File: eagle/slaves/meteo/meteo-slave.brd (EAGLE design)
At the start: 49.5 x 49.5 mm, 38 parts, among them CON1 SPI, IC1 MCP1703CB, J2 RJ12RIGHTANGLE-I2C, J3 RJ12RIGHTANGLE-I2C, U1 ATMEGA328P_TQFP, X1 8MHz, X2 1503_09, X3 1503_09

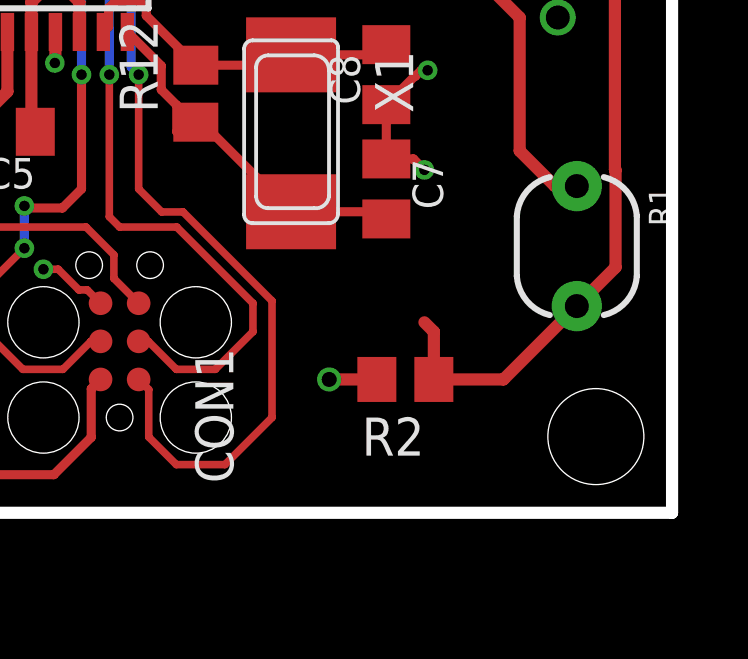
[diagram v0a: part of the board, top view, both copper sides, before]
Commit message: meteo-slave: change light control to use internal pullup
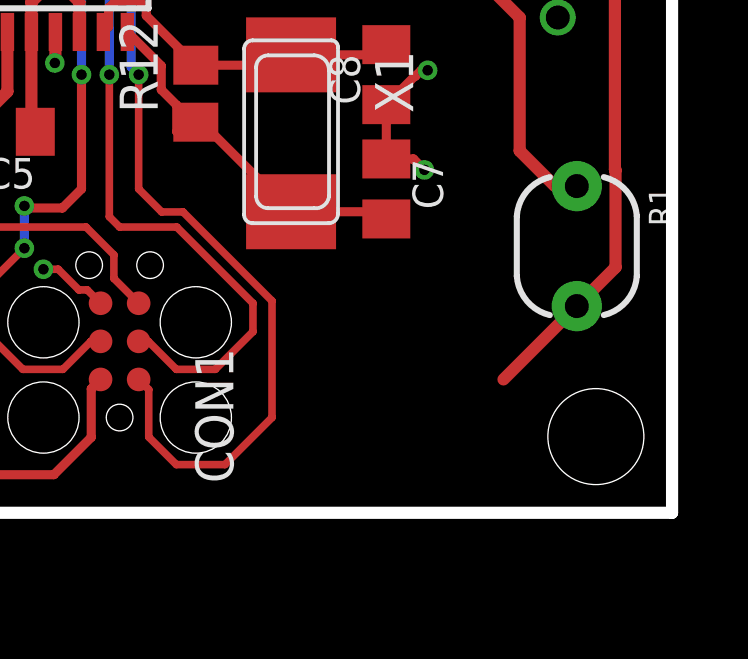
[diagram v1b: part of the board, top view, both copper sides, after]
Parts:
- removed R2: 10k, resistor:R0805
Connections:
- net A0: no longer R2.1
- net D5: no longer R1.1
- net GND: now also R1.1; no longer R2.2
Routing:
- net A0: track 54.2 -> 49.8 mm
- net GND: track 32.5 -> 30.9 mm, vias 12 -> 11
- net D5: track 18.8 -> 18.1 mm
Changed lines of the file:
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@@
 </element>
 <element name="R1" library="SparkFun" package="PHOTOCELL" value="PHOTOCELLPTH" x="46.355" y="8.89" rot="R270"/>
-<element name="R2" library="resistor" library_urn="urn:adsk.eagle:library:348" package="R0805" value="10k" x="40.64" y="4.445" rot="R180"/>
 <element name="U$1" library="Ava" package="DS1820" value="DS1820TO92" x="46.99" y="40.64" rot="R270"/>
 <element name="R4" library="resistor" library_urn="urn:adsk.eagle:library:348" package="R0805" value="4.7k" x="45.72" y="33.02" smashed="yes">
@@
 <contactref element="U$1" pad="GND"/>
 <contactref element="U2" pad="GND"/>
-<contactref element="R2" pad="2"/>
 <contactref element="U$19" pad="GND"/>
 <contactref element="X2" pad="3"/>
@@
 <wire x1="42.529" y1="20.336" x2="42.545" y2="20.32" width="0.4064" layer="1"/>
 <via x="42.545" y="20.32" extent="1-16" drill="0.5"/>
-<wire x1="39.69" y1="4.445" x2="38.1" y2="4.445" width="0.4064" layer="1"/>
-<via x="38.1" y="4.445" extent="1-16" drill="0.5"/>
 <wire x1="7.874" y1="39.37" x2="7.874" y2="37.719" width="0.4064" layer="1"/>
 <wire x1="7.874" y1="37.719" x2="7.62" y2="37.465" width="0.4064" layer="1"/>
@@
 <contactref element="R19" pad="1"/>
 <contactref element="C11" pad="1"/>
+<contactref element="R1" pad="1"/>
 <wire x1="41.245" y1="38.36" x2="45.72" y2="40.005" width="0" layer="19" extent="1-1"/>
 <wire x1="29.21" y1="31.877" x2="41.245" y2="38.36" width="0" layer="19" extent="16-16"/>
@@
 <wire x1="24.13" y1="4.445" x2="28.575" y2="8.1188" width="0" layer="19" extent="1-1"/>
 <wire x1="21.59" y1="4.445" x2="24.13" y2="4.445" width="0" layer="19" extent="1-1"/>
-<wire x1="38.1" y1="4.445" x2="30.48" y2="6.985" width="0" layer="19" extent="1-1"/>
-<wire x1="41.275" y1="11.43" x2="39.69" y2="4.445" width="0" layer="19" extent="1-1"/>
+<wire x1="6.745" y1="16.51" x2="16.51" y2="19.685" width="0" layer="19" extent="1-1"/>
+<wire x1="6.745" y1="14.47" x2="6.745" y2="16.51" width="0" layer="19" extent="1-1"/>
+<wire x1="40.005" y1="11.795" x2="30.48" y2="6.985" width="0" layer="19" extent="1-1"/>
 <wire x1="45.72" y1="16.51" x2="41.3824" y2="14.7506" width="0" layer="19" extent="1-1"/>
 <wire x1="42.545" y1="20.32" x2="45.72" y2="16.51" width="0" layer="19" extent="1-1"/>
-<wire x1="6.745" y1="16.51" x2="16.51" y2="19.685" width="0" layer="19" extent="1-1"/>
-<wire x1="6.745" y1="14.47" x2="6.745" y2="16.51" width="0" layer="19" extent="1-1"/>
+<wire x1="46.355" y1="10.89" x2="41.275" y2="11.43" width="0" layer="19" extent="1-1"/>
 <wire x1="6.745" y1="30.345" x2="18.1" y2="23.03" width="0" layer="19" extent="1-1"/>
 <wire x1="6.745" y1="32.385" x2="6.745" y2="30.345" width="0" layer="19" extent="1-1"/>
@@
 <contactref element="U1" pad="23"/>
 <contactref element="R1" pad="2"/>
-<contactref element="R2" pad="1"/>
-<wire x1="41.59" y1="4.445" x2="43.91" y2="4.445" width="0.4064" layer="1"/>
 <wire x1="43.91" y1="4.445" x2="46.355" y2="6.89" width="0.4064" layer="1"/>
-<wire x1="41.59" y1="4.445" x2="41.59" y2="6.035" width="0.4064" layer="1"/>
-<wire x1="41.59" y1="6.035" x2="41.275" y2="6.35" width="0.4064" layer="1"/>
 <wire x1="47.6464" y1="11.42491875" x2="47.625" y2="11.44631875" width="0.4064" layer="1"/>
 <wire x1="47.625" y1="11.44631875" x2="47.625" y2="26.67" width="0.4064" layer="1"/>
@@
 <signal name="D5">
 <contactref element="U1" pad="9"/>
-<contactref element="R1" pad="1"/>
 <wire x1="32.8676" y1="17.52" x2="43.44" y2="17.52" width="0.4064" layer="1"/>
 <wire x1="44.45" y1="16.51" x2="44.45" y2="12.065" width="0.4064" layer="1"/>
 <wire x1="44.45" y1="12.065" x2="45.625" y2="10.89" width="0.4064" layer="1"/>
-<wire x1="45.625" y1="10.89" x2="46.355" y2="10.89" width="0.4064" layer="1"/>
 <wire x1="43.44" y1="17.52" x2="44.45" y2="16.51" width="0.4064" layer="1"/>
 </signal>
